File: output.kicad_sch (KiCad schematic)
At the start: 27 parts, among them J9 Conn_01x03, U9 ULN2803A

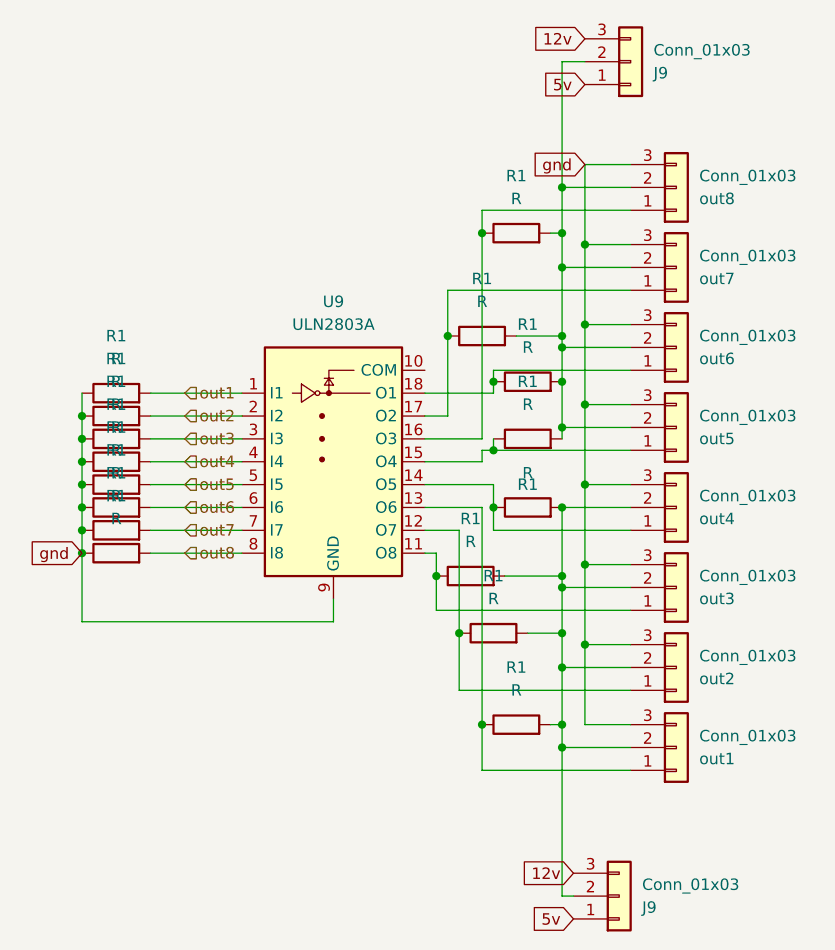
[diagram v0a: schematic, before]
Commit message: fixing labels / add some values
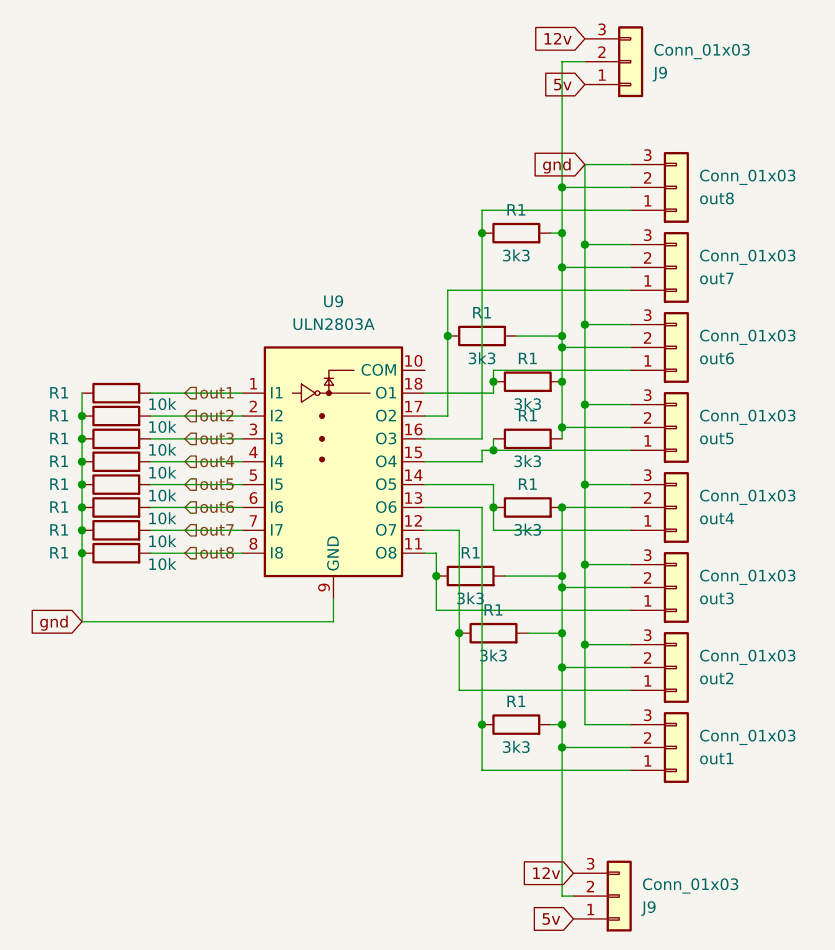
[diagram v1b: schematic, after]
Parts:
- R1: value R -> 10k
- R1: value R -> 3k3
